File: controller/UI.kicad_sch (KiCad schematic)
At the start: 4 parts

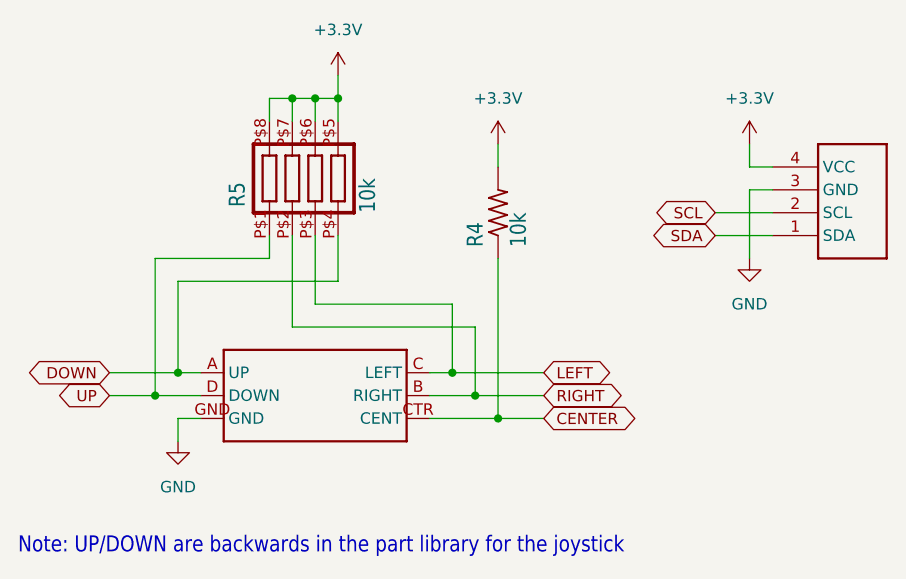
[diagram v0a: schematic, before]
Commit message: Cleaned up controller
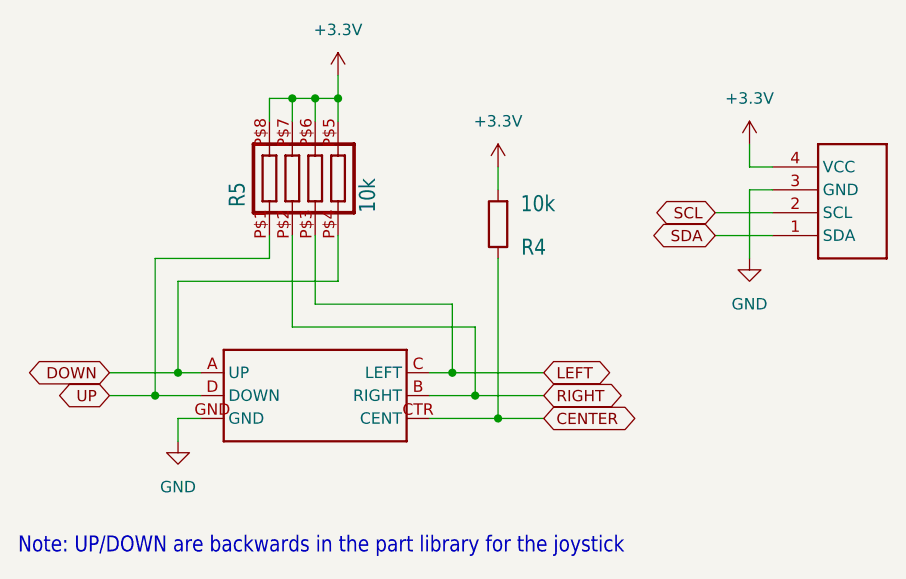
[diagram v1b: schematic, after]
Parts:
- R4: symbol controller-eagle-import:R-US_R0805 -> Device:R
- R5: symbol controller-eagle-import:744C083 -> controller:744C083
- S1: symbol controller-eagle-import:JOYSTICK_MINI -> controller:JOYSTICK_MINI
- U$5: symbol controller-eagle-import:SSD1306-OLED -> controller:SSD1306-OLED
